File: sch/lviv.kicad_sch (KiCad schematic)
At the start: 0 parts

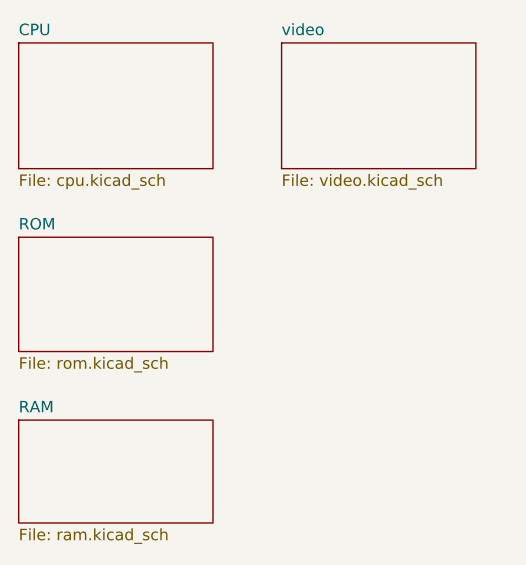
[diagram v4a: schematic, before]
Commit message: Sch: added PIO sheet
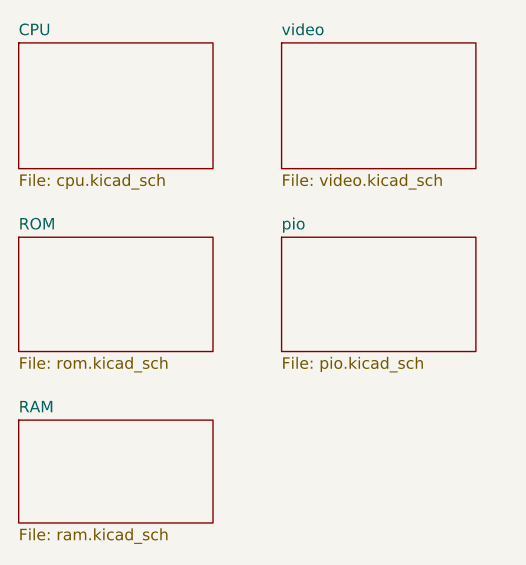
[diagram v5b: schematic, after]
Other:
- added sheet pio (pio.kicad_sch)
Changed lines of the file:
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@@
+    )
+  )
+  (sheet (at 73.66 49.53) (size 21.59 12.7) (fields_autoplaced)
+    (stroke (width 0.1524) (type solid) (color 0 0 0 0))
+    (fill (color 0 0 0 0.0000))
+    (property "Sheet name" "pio" (id 0) (at 73.66 48.8184 0)
+      (effects (font (size 1.27 1.27)) (justify left bottom))
+    )
+    (property "Sheet file" "pio.kicad_sch" (id 1) (at 73.66 62.8146 0)
+      (effects (font (size 1.27 1.27)) (justify left top))
     )
   )
@@
     (path "/e9506136-80e5-4250-83e4-52799f917e83" (page "4"))
     (path "/036afffe-cbbf-4ead-9c0c-ea4c435dd04c" (page "5"))
+    (path "/bc747cd9-2c14-4e8d-af52-0eda425fcd05" (page "6"))
   )
   (symbol_instances
@@
       (reference "#PWR?") (unit 1) (value "+5V") (footprint "")
     )
+    (path "/bc747cd9-2c14-4e8d-af52-0eda425fcd05/0ceff678-fdd5-4844-b0e6-b9747faf23be"
+      (reference "#PWR?") (unit 1) (value "GND") (footprint "")
+    )
     (path "/39367e70-4fd8-4578-b7c9-16f6f15e83e4/1238fc37-b0ef-40ea-80c5-a10ab39725c3"
       (reference "#PWR?") (unit 1) (value "GND") (footprint "")
@@
     )
     (path "/ec5c2062-3a41-4636-8803-069e60a1641a/2209ee81-6409-4c18-b0f0-f2ebfef5bc4a"
+      (reference "#PWR?") (unit 1) (value "+5V") (footprint "")
+    )
+    (path "/bc747cd9-2c14-4e8d-af52-0eda425fcd05/2507031b-f5f8-4904-8f00-05c1469bcb72"
       (reference "#PWR?") (unit 1) (value "+5V") (footprint "")
     )
@@
       (reference "#PWR?") (unit 1) (value "+12V") (footprint "")
     )
+    (path "/bc747cd9-2c14-4e8d-af52-0eda425fcd05/46b26e3f-0d19-4a34-bfd0-b2d3e83b634d"
+      (reference "#PWR?") (unit 1) (value "+5V") (footprint "")
+    )
     (path "/036afffe-cbbf-4ead-9c0c-ea4c435dd04c/4b5ea97b-e6aa-4fa8-ae11-6542bd1bd454"
       (reference "#PWR?") (unit 1) (value "+5V") (footprint "")
     )
+    (path "/bc747cd9-2c14-4e8d-af52-0eda425fcd05/4e67e9f1-95ee-42b5-8432-37d18e670075"
+      (reference "#PWR?") (unit 1) (value "GND") (footprint "")
+    )
     (path "/39367e70-4fd8-4578-b7c9-16f6f15e83e4/4e7eed74-a983-45cb-9e03-b393f9cad20a"
       (reference "#PWR?") (unit 1) (value "~") (footprint "")
     )
+    (path "/bc747cd9-2c14-4e8d-af52-0eda425fcd05/4eae17d9-f94c-4859-8090-e9273f036da2"
+      (reference "#PWR?") (unit 1) (value "+5V") (footprint "")
+    )
     (path "/ec5c2062-3a41-4636-8803-069e60a1641a/4f6e87d5-5020-4d60-91cb-aff01d599304"
       (reference "#PWR?") (unit 1) (value "+5V") (footprint "")
@@
       (reference "#PWR?") (unit 1) (value "~") (footprint "")
     )
+    (path "/bc747cd9-2c14-4e8d-af52-0eda425fcd05/7c2de4e1-f3a4-4280-8956-be02686efcce"
+      (reference "#PWR?") (unit 1) (value "GND") (footprint "")
+    )
     (path "/ec5c2062-3a41-4636-8803-069e60a1641a/850ce0f9-8cd8-4855-a5ee-8aeb731b2378"
       (reference "#PWR?") (unit 1) (value "~") (footprint "")
     )
+    (path "/bc747cd9-2c14-4e8d-af52-0eda425fcd05/866f5a6e-d351-428f-979e-3ad6d068b39c"
+      (reference "#PWR?") (unit 1) (value "GND") (footprint "")
+    )
     (path "/ec5c2062-3a41-4636-8803-069e60a1641a/8bcc7d2b-c179-4fd3-b6c9-041bfc176927"
       (reference "#PWR?") (unit 1) (value "GND") (footprint "")
@@
       (reference "#PWR?") (unit 1) (value "GND") (footprint "")
     )
+    (path "/bc747cd9-2c14-4e8d-af52-0eda425fcd05/d2963af2-40ca-4dbc-9265-52c3ea0d41ed"
+      (reference "#PWR?") (unit 1) (value "GND") (footprint "")
+    )
     (path "/ec5c2062-3a41-4636-8803-069e60a1641a/d4bee014-a77d-4f28-8a6e-bd217537f5f0"
       (reference "#PWR?") (unit 1) (value "+5V") (footprint "")
@@
       (reference "#PWR?") (unit 1) (value "GND") (footprint "")
     )
+    (path "/bc747cd9-2c14-4e8d-af52-0eda425fcd05/e27bb937-6e48-4025-8825-b280cac03461"
+      (reference "#PWR?") (unit 1) (value "GND") (footprint "")
+    )
     (path "/ec5c2062-3a41-4636-8803-069e60a1641a/e30d07a9-ad29-4cbe-a223-85bcb488d3e0"
       (reference "#PWR?") (unit 1) (value "GND") (footprint "")
@@
     (path "/39367e70-4fd8-4578-b7c9-16f6f15e83e4/f486d39b-03a2-4981-9e66-2d370c64d806"
       (reference "#PWR?") (unit 1) (value "~") (footprint "")
+    )
+    (path "/bc747cd9-2c14-4e8d-af52-0eda425fcd05/fbd8ef26-45b5-44ce-bf9a-1a688a7a611d"
+      (reference "#PWR?") (unit 1) (value "+5V") (footprint "")
     )
     (path "/39367e70-4fd8-4578-b7c9-16f6f15e83e4/ff553f31-1684-4de2-8b1b-396c089a5cc2"
@@
       (reference "D17") (unit 1) (value "2716") (footprint "")
     )
+    (path "/bc747cd9-2c14-4e8d-af52-0eda425fcd05/e0ae035f-3c19-4c84-8f48-c368909f211f"
+      (reference "D28") (unit 1) (value "74155") (footprint "")
+    )
     (path "/036afffe-cbbf-4ead-9c0c-ea4c435dd04c/740ac3f8-0b8d-487f-88b5-1d409ac88bb1"
       (reference "D29") (unit 1) (value "7401") (footprint "")
@@
       (reference "D29") (unit 2) (value "7401") (footprint "")
     )
+    (path "/bc747cd9-2c14-4e8d-af52-0eda425fcd05/cd256dab-518c-49d9-b20d-c55e20d238e4"
+      (reference "D30") (unit 1) (value "8255") (footprint "")
+    )
+    (path "/bc747cd9-2c14-4e8d-af52-0eda425fcd05/9e10d7da-7e44-4b95-bd4e-24e1819e2ea4"
+      (reference "D31") (unit 1) (value "8286") (footprint "")
+    )
+    (path "/bc747cd9-2c14-4e8d-af52-0eda425fcd05/0fa1ac02-8c11-40fa-9603-c934a83e4b4f"
+      (reference "D32") (unit 1) (value "8226") (footprint "")
+    )
     (path "/036afffe-cbbf-4ead-9c0c-ea4c435dd04c/027a9fdf-d4cf-4a2f-8554-9eccd8e22f97"
